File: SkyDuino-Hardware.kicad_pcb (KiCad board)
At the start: 4 copper layers, 123 x 56 mm, 80 parts, among them J1 24V, J11 DBG, J12 USB-A RMT, J13 DISP, J14 USB_C Artisan, J2 BT, J4 Drum, J5 Exhaust, J6 Cooling, J7 Cooling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

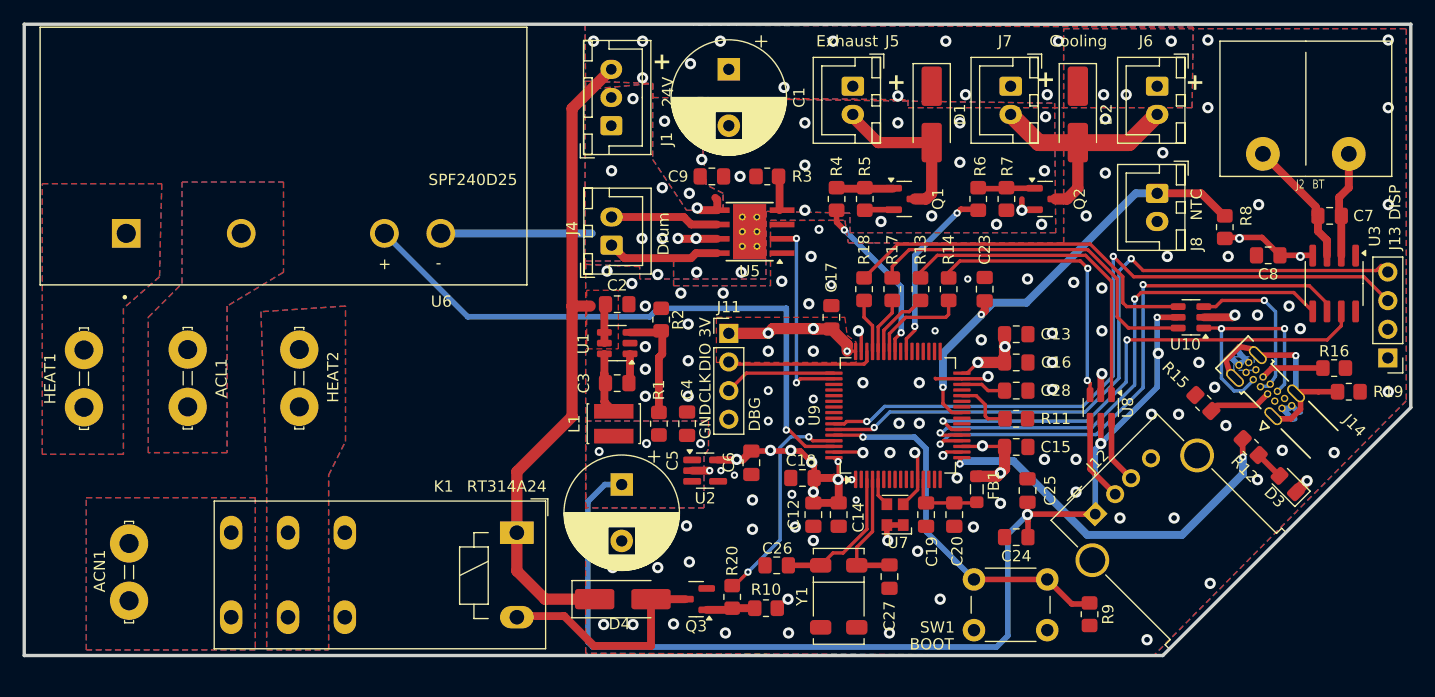
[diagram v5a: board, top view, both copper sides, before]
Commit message: Fix DRC vialations
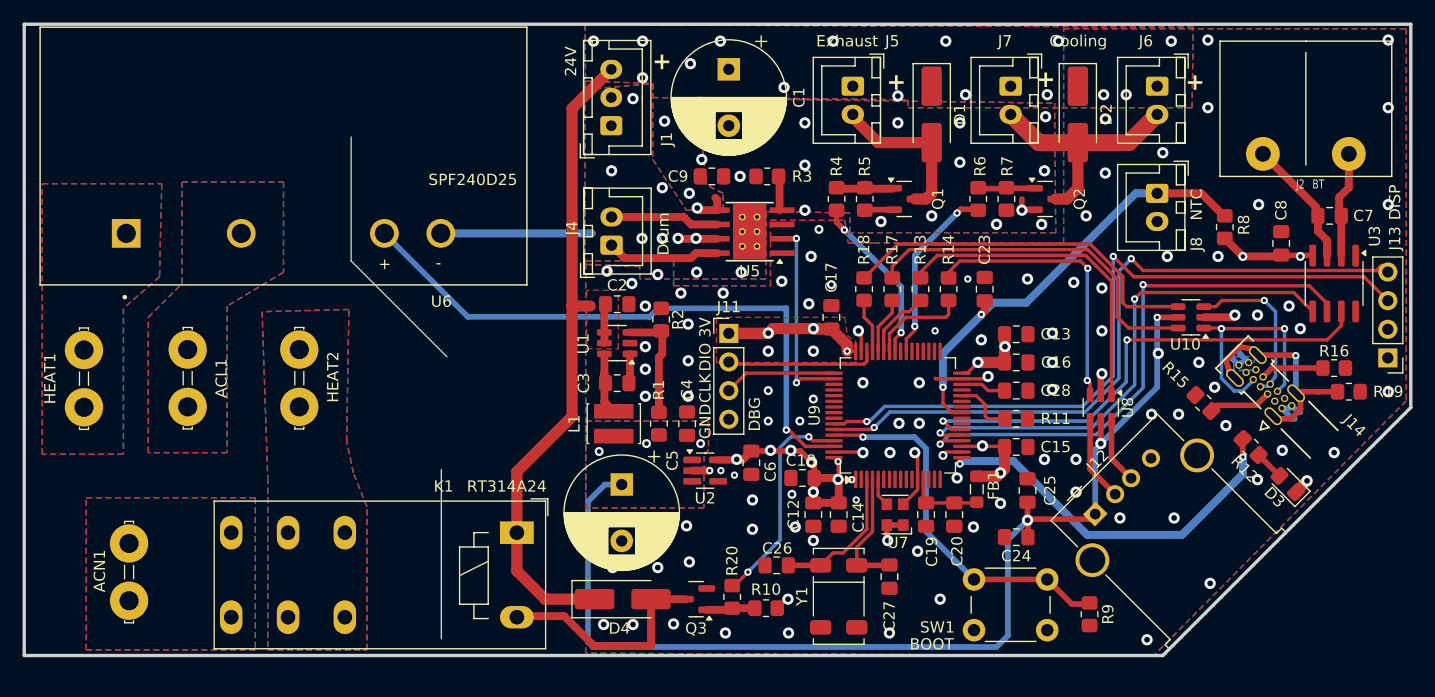
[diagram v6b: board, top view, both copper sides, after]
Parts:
- moved C8 1.57 mm to (217.5, 99.4), turned to 90 degrees
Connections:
- K1 pad 12: unconnected-(K1-Pad12)_0 -> Net-(HEAT2-Pin_1)
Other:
- outline, holes or cut-outs redrawn

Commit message: Use VBus for 3V3 LDO
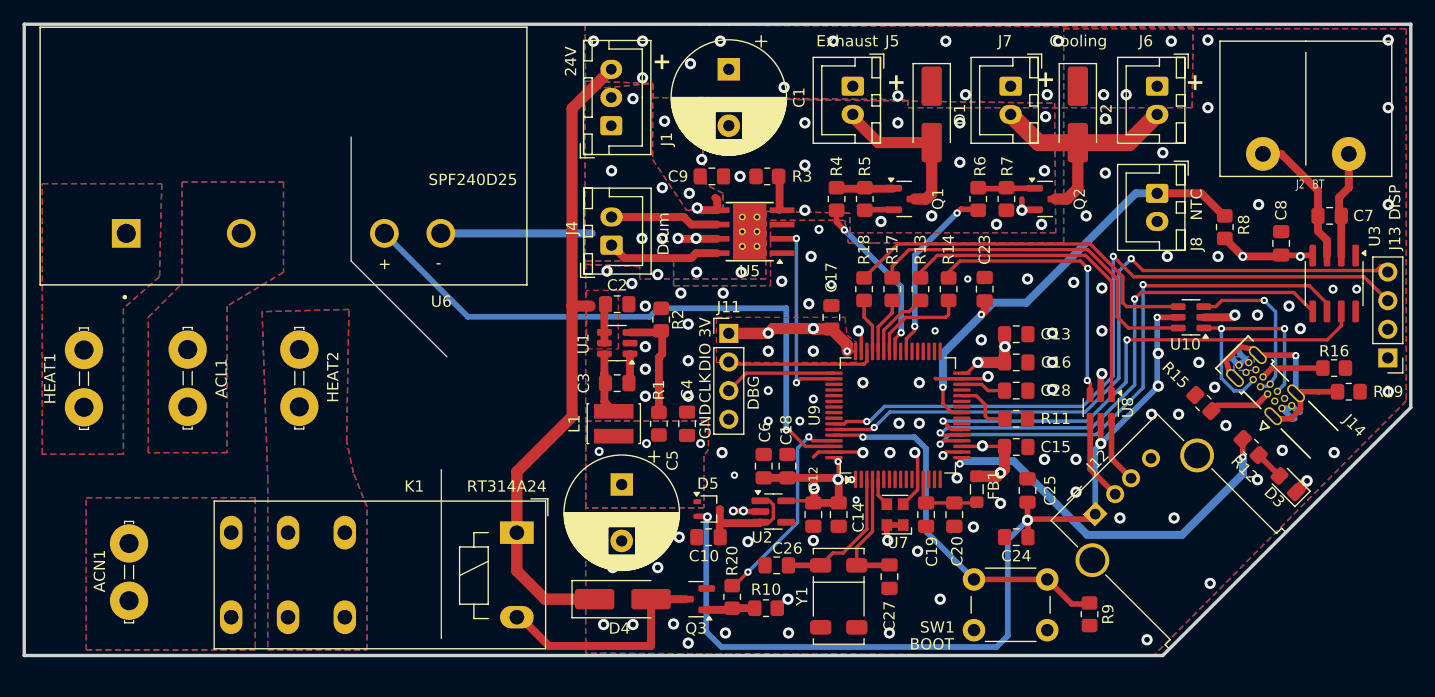
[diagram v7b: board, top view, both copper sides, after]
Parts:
- added C10: 22µF, Capacitor_SMD:C_0805_2012Metric_Pad1.18x1.45mm_HandSolder, F.Cu at (166.7, 125.5)
- added D5: BAT54CWFILMY, Package_TO_SOT_SMD:SOT-323_SC-70, F.Cu at (166.7, 123.0)
- moved U2 7.05 mm to (172.4, 123.2)
- moved C18 1.70 mm to (173.7, 119.2), turned to 90 degrees
- moved C6 1.14 mm to (171.6, 119.2), turned to 90 degrees
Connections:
- C24 pad 1: +5V -> VBUS
- C25 pad 1: +5V -> VBUS
- J12 pad 1: +5V -> VBUS
- J13 pad 2: +5V -> VBUS
- J14 pad A4: unconnected-(J14-VBUS-PadA4) -> VBUS
- J14 pad A9: unconnected-(J14-VBUS-PadA9) -> VBUS
- J14 pad B4: unconnected-(J14-VBUS-PadB4) -> VBUS
- J14 pad B9: unconnected-(J14-VBUS-PadB9) -> VBUS
- U10 pad 5: +5V -> VBUS
- U2 pad 1: +5V -> Net-(U2-CTRL)
- U2 pad 3: +5V -> Net-(U2-CTRL)
- U8 pad 5: +5V -> VBUS
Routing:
- net VBUS: track 0.00 -> 120.9 mm, vias 0 -> 6
- net +5V: track 119.8 -> 0.48 mm, vias 7 -> 3
- net Net-(U2-CTRL): track 0.00 -> 9.16 mm
- net +3V3: track 64.1 -> 60.5 mm, vias 20 -> 16
- net GND: track 50.9 -> 53.7 mm
- net Net-(J2-Pin_1): track 11.3 -> 12.3 mm
- net HEAT_CTL: track 19.4 -> 18.5 mm
